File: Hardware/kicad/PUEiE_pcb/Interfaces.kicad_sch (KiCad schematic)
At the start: 9 parts, among them U2 MAX-M10S-00B

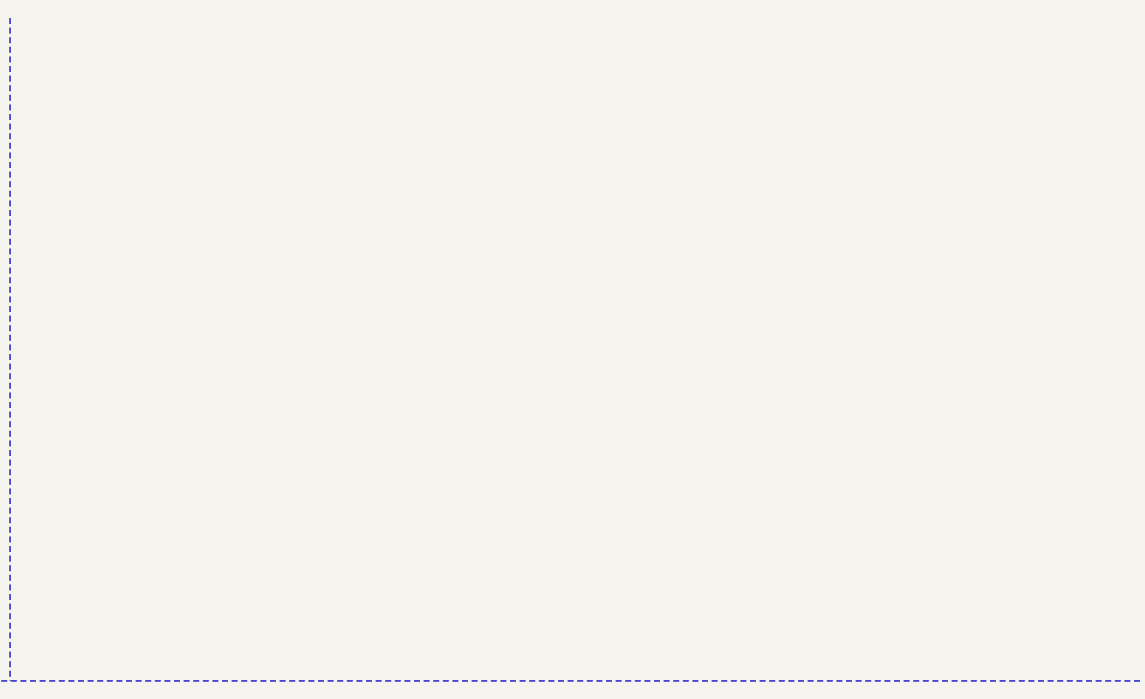
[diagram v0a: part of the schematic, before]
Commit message: magnetometer ,stepper controller
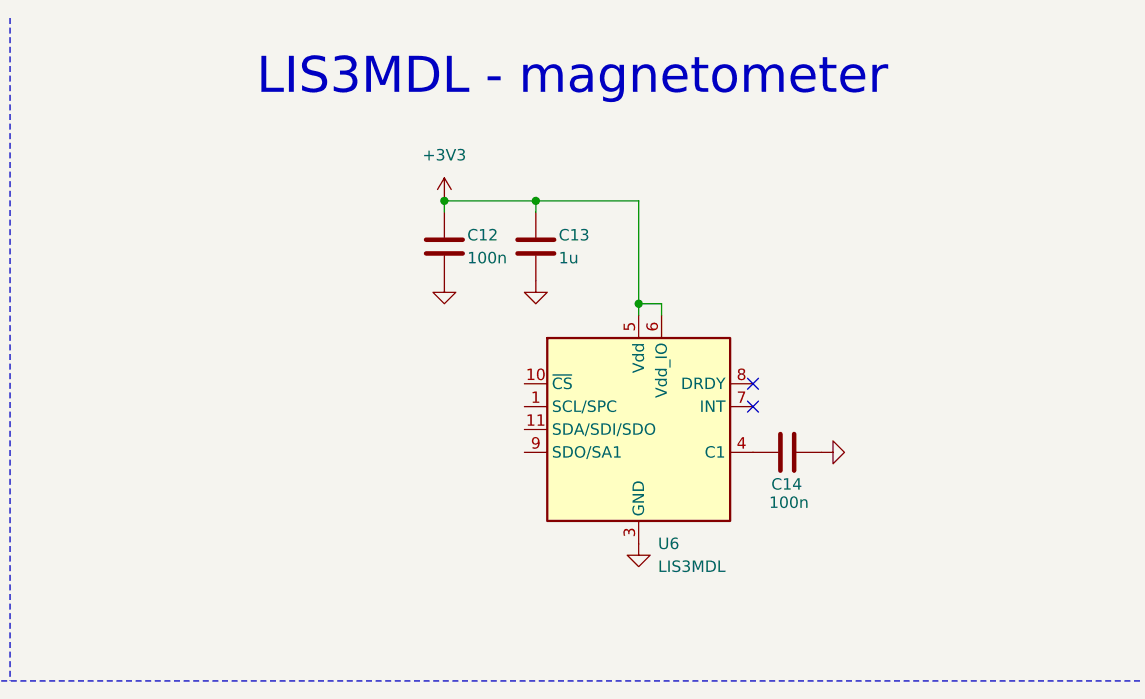
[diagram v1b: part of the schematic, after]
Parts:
- added C12, C14: 100n, Capacitor_SMD:C_0805_2012Metric, symbol Device:C
- added C13: 1u, Capacitor_SMD:C_0805_2012Metric, symbol Device:C
- added U6: LIS3MDL, Package_LGA:LGA-12_2x2mm_P0.5mm, symbol Sensor_Magnetic:LIS3MDL
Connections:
- net +3V3: now also C12.1, C13.1, U6.5 (Vdd), U6.6 (Vdd_IO)
- net GND: now also C12.2, C13.2, C14.1, U6.12 (GND), U6.2 (GND), U6.3 (GND)
- new net: C14.2, U6.4 (C1)
- no-connect marks 7 -> 9
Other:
- note added: "LIS3MDL - magnetometer"

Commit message: stm32WB55
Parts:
- added C15: 22n, Capacitor_SMD:C_0805_2012Metric, symbol Device:C
- added C16, C17, C19, C23: 100n, Capacitor_SMD:C_0805_2012Metric, symbol Device:C
- added C18: 2.2u, Capacitor_SMD:C_0805_2012Metric, symbol Device:C
- added C20: 1u, Capacitor_SMD:C_0805_2012Metric, symbol Device:C
- added C21, C22, C26: 10u, Capacitor_SMD:C_0805_2012Metric, symbol Device:C
- added C24, C25: 100u, symbol Device:C_Polarized
- added D4: ESD131-B1-W0201, Diode_SMD:Infineon_SG-WLL-2-3_0.58x0.28_P0.36mm, symbol Diode:ESD131-B1-W0201
- added J2: Conn_01x04_Socket, symbol Connector:Conn_01x04_Socket
- added JP3, JP4, JP5, JP6: SolderJumper_2_Open, symbol Jumper:SolderJumper_2_Open
- added L3: 2.7n, symbol Device:L
- added R11: 10, Resistor_SMD:R_0805_2012Metric, symbol Device:R
- added R7, R9: 0.1, Resistor_SMD:R_1206_3216Metric, symbol Device:R
- added U4: TMC2208-LA, Package_DFN_QFN:TQFN-32-1EP_5x5mm_P0.5mm_EP3.4x3.4mm_ThermalVias, symbol Driver_Motor:TMC2208-LA
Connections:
- net +3V3: now also C16.1, JP6.1 (A), U4.15 (VCC_IO)
- net GND: now also C16.2, C17.2, C18.2, C20.2, C21.2, C22.2, C23.2, C24.2, C25.2, C26.2, D4.1 (A1), JP3.1 (A), JP4.1 (A), R7.1, R9.1, U4.13 (CLK), U4.18 (GND), U4.3 (GND)
- net at AE1.1 (A), U2.11 (RF_IN): now also D4.2 (A2), L3.2
- net at U2.14 (VCC_RF): now also R11.1
- new net: J2.1 (Pin_1), U4.1 (OB2)
- new net: J2.2 (Pin_2), U4.26 (OB1)
- new net: J2.3 (Pin_3), U4.21 (OA2)
- new net: J2.4 (Pin_4), U4.24 (OA1)
- new net: JP3.2 (B), R7.2, U4.23 (BRA)
- new net: JP5.2 (B), U4.10 (MS2)
- new net: C19.2, U4.6 (VCP)
- new net: C26.1, L3.1, R11.2
- new net: JP4.2 (B), R9.2, U4.27 (BRB)
- new net: C15.2, U4.4 (CPO)
- new net: C15.1, U4.5 (CPI)
- new net: C18.1, U4.8 (5VOUT)
- new net: JP6.2 (B), U4.9 (MS1)
- new net +Vbat_fuse: C17.1, C19.1, C20.1, C21.1, C22.1, C23.1, C24.1, C25.1, U4.22 (VS), U4.28 (VS)
- new net DIR: U4.19 (DIR)
- new net ENN: U4.2 (ENN)
- new net STEP: U4.16 (STEP)
- no-connect marks 9 -> 13
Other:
- note added: "Stepper Motor Driver"
- moved on the sheet: AE1

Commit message: stm32WB
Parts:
- removed R12, R13: 100k, Resistor_SMD:R_0805_2012Metric, symbol Device:R
- added C317: 100n, Capacitor_SMD:C_0805_2012Metric, symbol Device:C
- added J302: Conn_01x04, symbol Connector_Generic:Conn_01x04
- added R302, R303, R307: 10k, Resistor_SMD:R_0201_0603Metric, symbol Device:R
- R301: renamed from R11; value 10 -> 10R
- renumbered AE1 to AE301, BT1 to BT301, C12 to C301, C13 to C302, C26 to C303, C14 to C304, C10 to C305, C24 to C306, C25 to C307, C17 to C308, C23 to C309, C22 to C310, C21 to C311, C20 to C312, C16 to C313, C19 to C314, C15 to C315, C18 to C316, D1 to D301, D4 to D302, J2 to J301, JP1 to JP301, JP6 to JP302, JP5 to JP303, JP3 to JP304, JP4 to JP305, L3 to L301, R10 to R304, R7 to R305, R9 to R306, U2 to U301, U6 to U302, U4 to U303
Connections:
- net +3V3: now also JP303.1 (A), C317.1, J302.1 (Pin_1), R307.1
- net GND: now also C317.2, J302.4 (Pin_4)
- net GPS_RESET: now also R307.2
- net RX: now also R302.2
- net TX: now also R303.2
- net at JP301.1 (A): now also R303.1
- net at JP301.3 (B): now also R302.1
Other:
- company: (none) -> Dominik Ledzianowski / Klaudia Lewandowska
- title: (none) -> Boat Autopilot Controller
- moved on the sheet: BT301, C305
